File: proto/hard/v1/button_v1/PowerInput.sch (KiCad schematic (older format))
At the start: 15 parts, among them J5 USB_B_Micro, U3 AP1117-33, U4 RT8009-33, U7 RClamp0554S

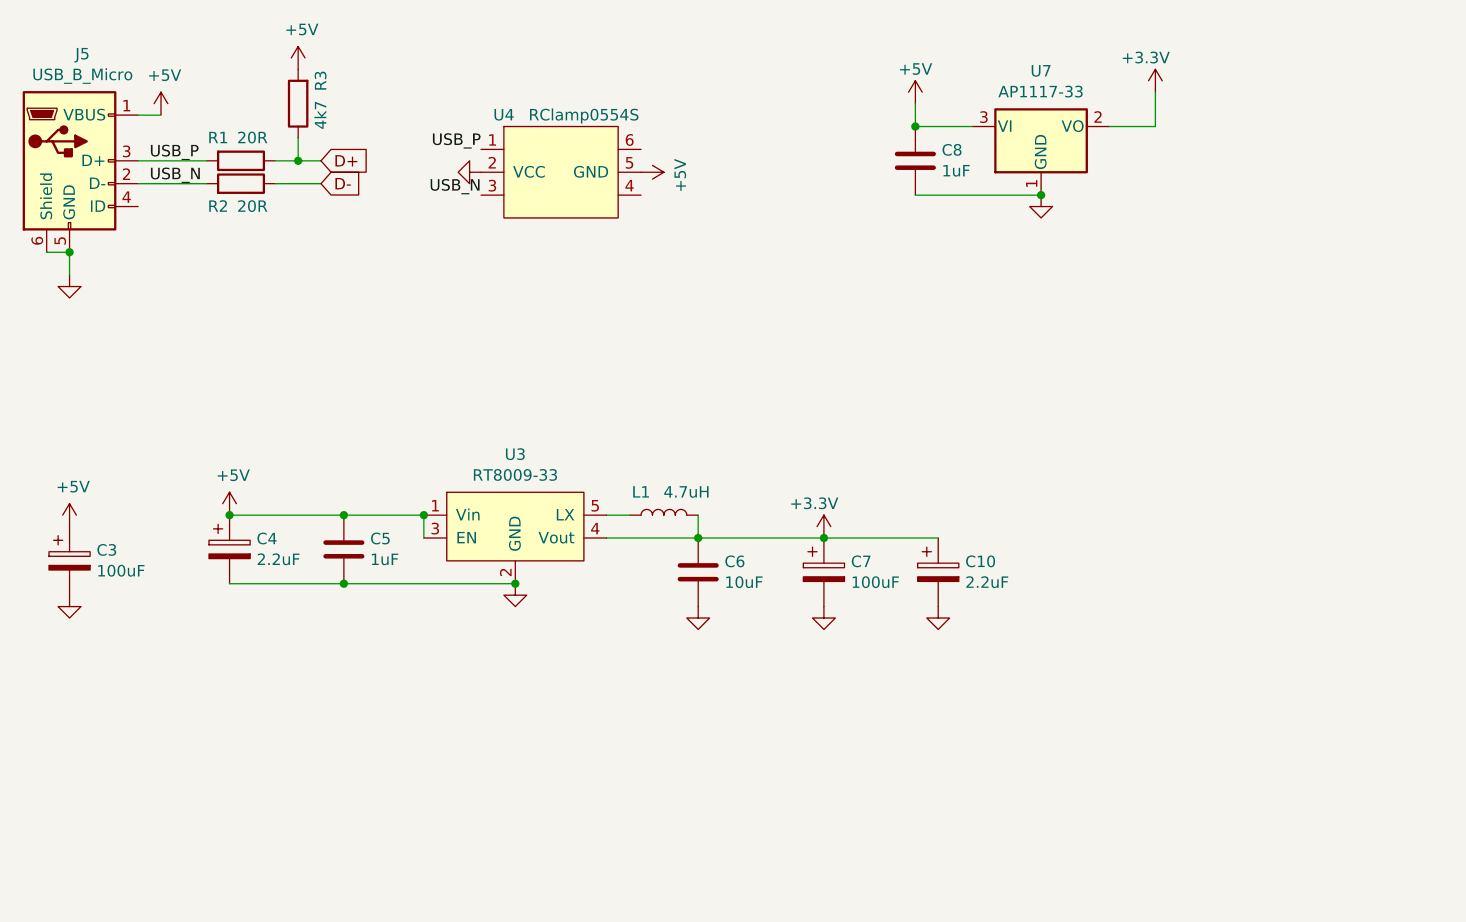
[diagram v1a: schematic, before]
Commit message: Fixed RClamp0554S wrong pinout. Corrected schematic and PCB. Added text for ICs on board.
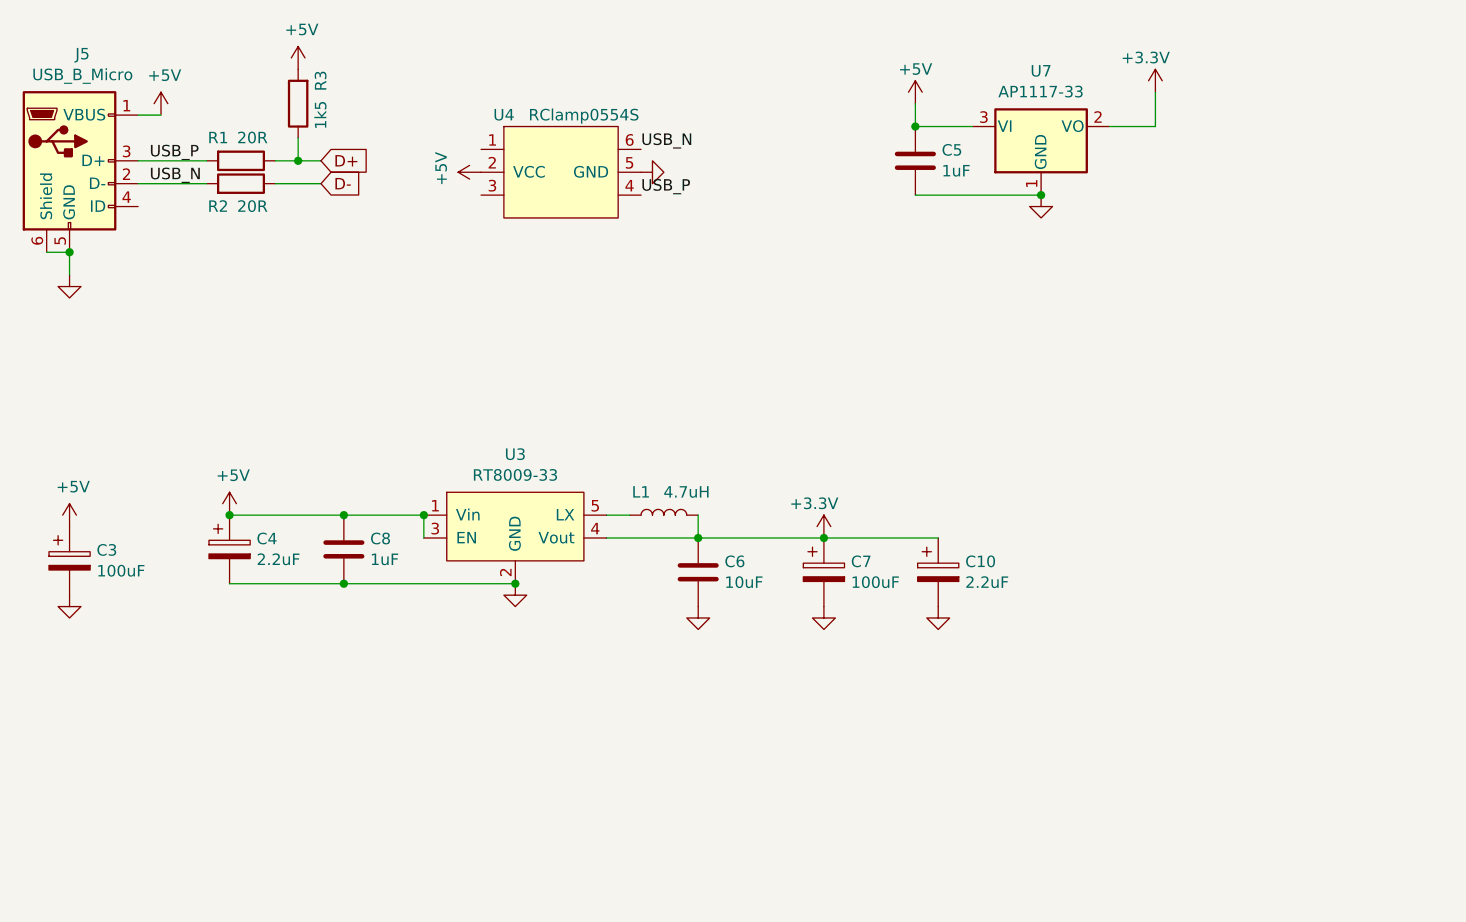
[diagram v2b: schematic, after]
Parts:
- R3: value 4k7 -> 1k5
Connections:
- net +5V: now also U7.2 (VCC); no longer U7.5 (GND)
- net GND: now also U7.5 (GND); no longer U7.2 (VCC)
- net USB_N: now also U7.6; no longer U7.3
- net USB_P: now also U7.4; no longer U7.1
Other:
- moved on the sheet: C5, C8
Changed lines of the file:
@@
 EESchema Schematic File Version 4
+LIBS:button_v1-cache
 EELAYER 29 0
 EELAYER END
@@
 AR Path="/5D4A520B/5D41A809" Ref="R3"  Part="1"
 F 0 "R3" V 2200 1150 50  0000 C CNN
-F 1 "4k7" V 2200 1300 50  0000 C CNN
+F 1 "1k5" V 2200 1300 50  0000 C CNN
 F 2 "Resistor_SMD:R_0805_2012Metric_Pad1.15x1.40mm_HandSolder" V 2230 1250 50  0001 C CNN
 F 3 "~" H 2300 1250 50  0001 C CNN
@@
 L power:GND #PWR?
 U 1 1 5D44DF1D
-P 3100 1550
+P 3800 1550
 AR Path="/5D44DF1D" Ref="#PWR?"  Part="1"
 AR Path="/5D1C99DD/5D44DF1D" Ref="#PWR0110"  Part="1"
 AR Path="/5D4A520B/5D44DF1D" Ref="#PWR0109"  Part="1"
-F 0 "#PWR0109" H 3100 1300 50  0001 C CNN
-F 1 "GND" H 3105 1377 50  0001 C CNN
+F 0 "#PWR0109" H 3800 1300 50  0001 C CNN
+F 1 "GND" H 3805 1377 50  0001 C CNN
+F 2 "" H 3800 1550 50  0001 C CNN
+F 3 "" H 3800 1550 50  0001 C CNN
+	1    3800 1550
+	0    -1   -1   0
+$EndComp
+$Comp
+L power:+5V #PWR?
+U 1 1 5D44DF23
+P 3100 1550
+AR Path="/5D44DF23" Ref="#PWR?"  Part="1"
+AR Path="/5D1C99DD/5D44DF23" Ref="#PWR0111"  Part="1"
+AR Path="/5D4A520B/5D44DF23" Ref="#PWR0110"  Part="1"
+F 0 "#PWR0110" H 3100 1400 50  0001 C CNN
+F 1 "+5V" H 3115 1723 50  0000 C CNN
 F 2 "" H 3100 1550 50  0001 C CNN
 F 3 "" H 3100 1550 50  0001 C CNN
 	1    3100 1550
-	0    1    1    0
-$EndComp
-$Comp
-L power:+5V #PWR?
-U 1 1 5D44DF23
-P 3800 1550
-AR Path="/5D44DF23" Ref="#PWR?"  Part="1"
-AR Path="/5D1C99DD/5D44DF23" Ref="#PWR0111"  Part="1"
-AR Path="/5D4A520B/5D44DF23" Ref="#PWR0110"  Part="1"
-F 0 "#PWR0110" H 3800 1400 50  0001 C CNN
-F 1 "+5V" H 3815 1723 50  0000 C CNN
-F 2 "" H 3800 1550 50  0001 C CNN
-F 3 "" H 3800 1550 50  0001 C CNN
-	1    3800 1550
-	0    1    1    0
-$EndComp
-Text Label 3100 1650 2    50   ~ 0
+	0    -1   -1   0
+$EndComp
+Text Label 3800 1450 0    50   ~ 0
 USB_N
-Text Label 3100 1450 2    50   ~ 0
+Text Label 3800 1650 0    50   ~ 0
 USB_P
 $Comp
@@
 L Device:C C?
 U 1 1 5D468D68
-P 5000 1500
+P 2500 3200
 AR Path="/5D468D68" Ref="C?"  Part="1"
 AR Path="/5D1C99DD/5D468D68" Ref="C7"  Part="1"
 AR Path="/5D4A520B/5D468D68" Ref="C8"  Part="1"
-F 0 "C8" H 5115 1546 50  0000 L CNN
-F 1 "1uF" H 5115 1455 50  0000 L CNN
-F 2 "Capacitor_SMD:C_0805_2012Metric_Pad1.15x1.40mm_HandSolder" H 5038 1350 50  0001 C CNN
-F 3 "~" H 5000 1500 50  0001 C CNN
-	1    5000 1500
+F 0 "C8" H 2615 3246 50  0000 L CNN
+F 1 "1uF" H 2615 3155 50  0000 L CNN
+F 2 "Capacitor_SMD:C_0805_2012Metric_Pad1.15x1.40mm_HandSolder" H 2538 3050 50  0001 C CNN
+F 3 "~" H 2500 3200 50  0001 C CNN
+	1    2500 3200
 	1    0    0    -1
 $EndComp
@@
 L Device:C C?
 U 1 1 5D48B2B1
-P 2500 3200
+P 5000 1500
 AR Path="/5D48B2B1" Ref="C?"  Part="1"
 AR Path="/5D1C99DD/5D48B2B1" Ref="C5"  Part="1"
 AR Path="/5D4A520B/5D48B2B1" Ref="C5"  Part="1"
-F 0 "C5" H 2615 3246 50  0000 L CNN
-F 1 "1uF" H 2615 3155 50  0000 L CNN
-F 2 "Capacitor_SMD:C_0805_2012Metric_Pad1.15x1.40mm_HandSolder" H 2538 3050 50  0001 C CNN
-F 3 "~" H 2500 3200 50  0001 C CNN
-	1    2500 3200
-	1    0    0    -1
-$EndComp
+F 0 "C5" H 5115 1546 50  0000 L CNN
+F 1 "1uF" H 5115 1455 50  0000 L CNN
+F 2 "Capacitor_SMD:C_0805_2012Metric_Pad1.15x1.40mm_HandSolder" H 5038 1350 50  0001 C CNN
+F 3 "~" H 5000 1500 50  0001 C CNN
+	1    5000 1500
+	1    0    0    -1
+$EndComp

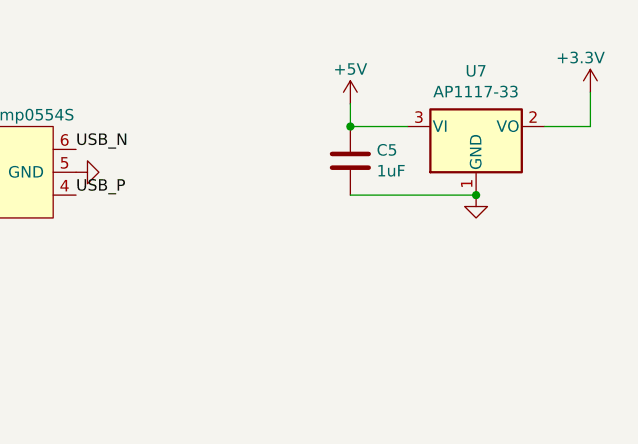
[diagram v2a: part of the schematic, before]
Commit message: Started schematic and PCB rework. Generated button_v1.pdf was left out of sync intentionally.
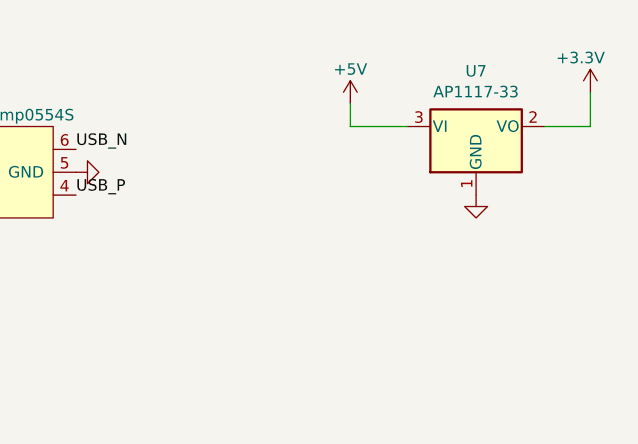
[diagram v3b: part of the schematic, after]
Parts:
- removed C5: 1uF, Capacitor_SMD:C_0805_2012Metric_Pad1.15x1.40mm_HandSolder, symbol Device:C
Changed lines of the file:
@@
 Wire Wire Line
 	5000 1250 5000 1350
-Connection ~ 5000 1350
-Wire Wire Line
-	5000 1650 5550 1650
-Connection ~ 5550 1650
 Wire Wire Line
 	5850 1350 6050 1350
@@
 	1    0    0    -1
 $EndComp
-$Comp
-L Device:C C?
-U 1 1 5D48B2B1
-P 5000 1500
-AR Path="/5D48B2B1" Ref="C?"  Part="1"
-AR Path="/5D1C99DD/5D48B2B1" Ref="C5"  Part="1"
-AR Path="/5D4A520B/5D48B2B1" Ref="C5"  Part="1"
-F 0 "C5" H 5115 1546 50  0000 L CNN
-F 1 "1uF" H 5115 1455 50  0000 L CNN
-F 2 "Capacitor_SMD:C_0805_2012Metric_Pad1.15x1.40mm_HandSolder" H 5038 1350 50  0001 C CNN
-F 3 "~" H 5000 1500 50  0001 C CNN
-	1    5000 1500
-	1    0    0    -1
-$EndComp

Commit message: Finished main board PCB
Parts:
- added Q9: TP0610T, Package_TO_SOT_SMD:SOT-23, symbol Transistor_FET:TP0610T
- added R14: 47k, Resistor_SMD:R_0805_2012Metric_Pad1.15x1.40mm_HandSolder, symbol Device:R
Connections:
- net +5V: now also Q9.2 (S), R14.1; no longer R3.2
- new net: Q9.3 (D), R3.2
- new net USB_PULLUP: Q9.1 (G), R14.2
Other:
- moved on the sheet: C10, C3, C4, C6, C7, C8, J5, L1, R1, R2, R3, U3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

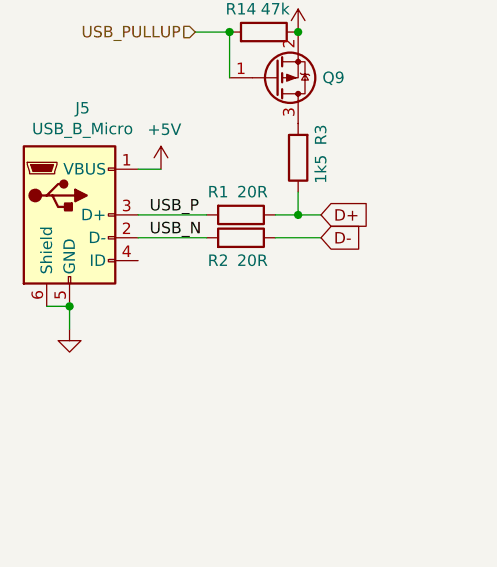
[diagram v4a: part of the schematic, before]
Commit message: Updated main board to v0.3: - changed power coils to bobbin - added test point for StartLED line - integrated new LCD screen footprint with LED power connectors - changed Schottky diode footprint to smaller in start LED converter - changed crystal footprint to smaller - added guard ring around crystal - disconnected USB shield from GND line
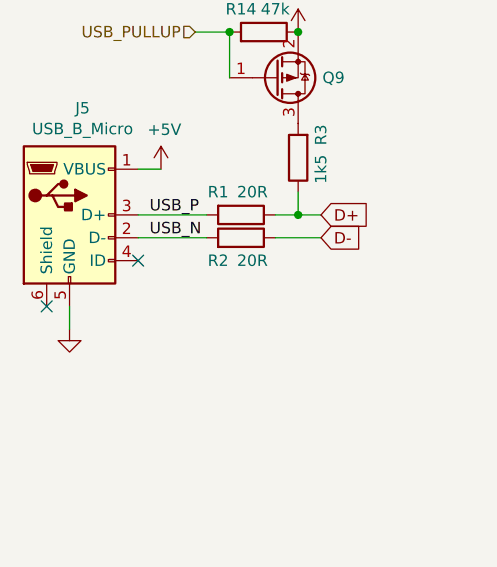
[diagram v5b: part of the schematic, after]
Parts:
- L1: footprint Inductor_SMD:L_0805_2012Metric_Pad1.15x1.40mm_HandSolder -> Inductor_SMD:L_Taiyo-Yuden_NR-50xx
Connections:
- net GND: no longer J5.6 (Shield)
- no-connect marks 0 -> 2
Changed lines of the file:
@@
 Wire Wire Line
 	1300 2650 1300 2550
-Wire Wire Line
-	1300 2550 1200 2550
-Connection ~ 1300 2550
 $Comp
 L power:+5V #PWR?
@@
 F 0 "L1" V 3950 4350 50  0000 C CNN
 F 1 "4.7uH" V 3950 4150 50  0000 C CNN
-F 2 "Inductor_SMD:L_0805_2012Metric_Pad1.15x1.40mm_HandSolder" H 3850 4250 50  0001 C CNN
+F 2 "Inductor_SMD:L_Taiyo-Yuden_NR-50xx" H 3850 4250 50  0001 C CNN
 F 3 "~" H 3850 4250 50  0001 C CNN
 	1    3850 4250
@@
 	1850 1350 2000 1350
 Connection ~ 2000 1350
+NoConn ~ 1600 2350
+NoConn ~ 1200 2550
 $EndSCHEMATC

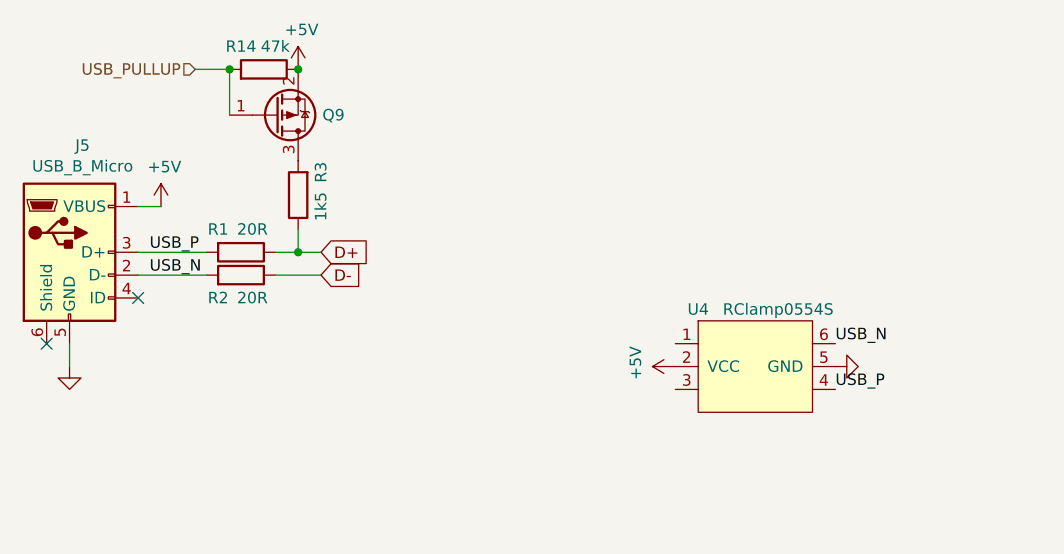
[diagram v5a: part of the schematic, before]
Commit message: Moved buttons to separate sheet. Added replacement transistors for buttons.
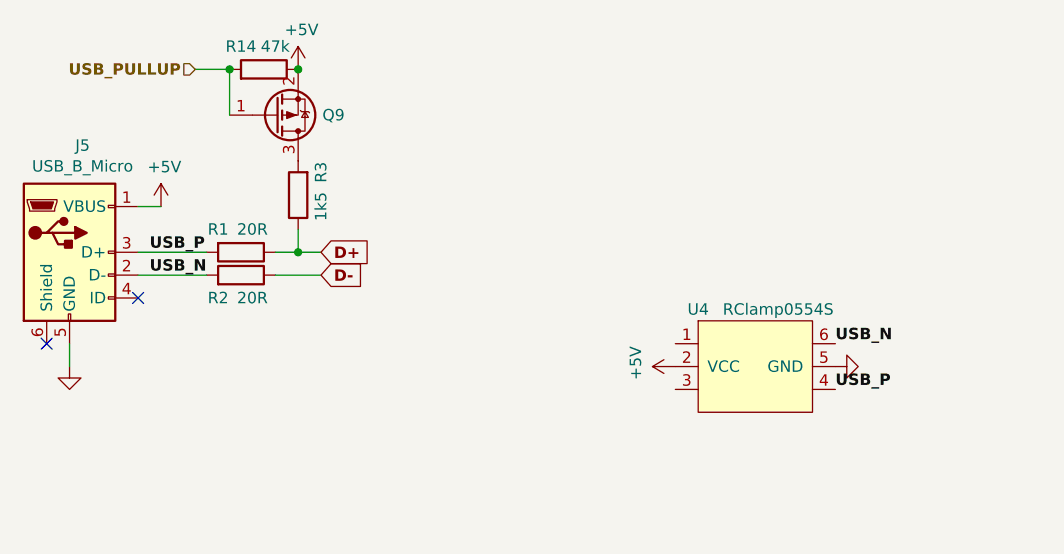
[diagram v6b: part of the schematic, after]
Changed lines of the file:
@@
 $Descr A4 11693 8268
 encoding utf-8
-Sheet 3 3
+Sheet 3 4
 Title ""
 Date ""
@@
 	1    0    0    -1
 $EndComp
-Text Label 1650 2150 0    50   ~ 0
+Text Label 1650 2150 0    50   ~ 6
 USB_P
-Text Label 1650 2250 0    50   ~ 0
+Text Label 1650 2250 0    50   ~ 6
 USB_N
 Wire Wire Line
@@
 Wire Wire Line
 	1600 2250 1900 2250
-Text GLabel 2400 2150 2    50   Input ~ 0
+Text GLabel 2400 2150 2    50   Input ~ 6
 D+
-Text GLabel 2400 2250 2    50   Input ~ 0
+Text GLabel 2400 2250 2    50   Input ~ 6
 D-
 $Comp
@@
 	0    -1   -1   0
 $EndComp
-Text Label 4650 2550 0    50   ~ 0
+Text Label 4650 2550 0    50   ~ 6
 USB_N
-Text Label 4650 2750 0    50   ~ 0
+Text Label 4650 2750 0    50   ~ 6
 USB_P
 $Comp
@@
 	1    0    0    -1
 $EndComp
-Text HLabel 1850 1350 0    50   Input ~ 0
+Text HLabel 1850 1350 0    50   Input ~ 6
 USB_PULLUP
 $Comp

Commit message: BOOT0 connected to GND Due to migration to Kicad V5.1.6 had to change text style from "bold" to "normal"
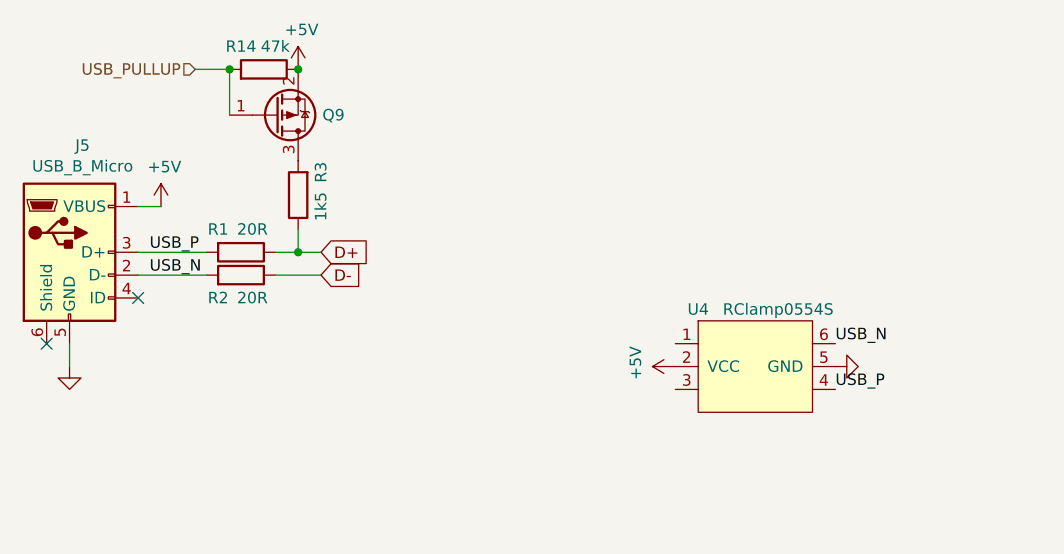
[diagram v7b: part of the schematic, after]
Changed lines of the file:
@@
 EESchema Schematic File Version 4
-LIBS:button_v1-cache
-EELAYER 29 0
+EELAYER 30 0
 EELAYER END
 $Descr A4 11693 8268
@@
 	1    0    0    -1
 $EndComp
-Text Label 1650 2150 0    50   ~ 6
+Text Label 1650 2150 0    50   ~ 0
 USB_P
-Text Label 1650 2250 0    50   ~ 6
+Text Label 1650 2250 0    50   ~ 0
 USB_N
 Wire Wire Line
@@
 Wire Wire Line
 	1600 2250 1900 2250
-Text GLabel 2400 2150 2    50   Input ~ 6
+Text GLabel 2400 2150 2    50   Input ~ 0
 D+
-Text GLabel 2400 2250 2    50   Input ~ 6
+Text GLabel 2400 2250 2    50   Input ~ 0
 D-
 $Comp
@@
 	0    -1   -1   0
 $EndComp
-Text Label 4650 2550 0    50   ~ 6
+Text Label 4650 2550 0    50   ~ 0
 USB_N
-Text Label 4650 2750 0    50   ~ 6
+Text Label 4650 2750 0    50   ~ 0
 USB_P
 $Comp
@@
 	1    0    0    -1
 $EndComp
-Text HLabel 1850 1350 0    50   Input ~ 6
+Text HLabel 1850 1350 0    50   Input ~ 0
 USB_PULLUP
 $Comp
